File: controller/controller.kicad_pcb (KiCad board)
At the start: 2 copper layers, 14 parts, among them SW1 SW_Push, SW2 SW_Push, SW3 SW_Push, SW4 SW_Push, U1 COM-09032, U2 COM-09032, U3 NRF24L01_Breakout

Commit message: [pcb] controller layout
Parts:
- moved SW2 89.8 mm to (141.4, 79.7)
- moved SW4 88.3 mm to (141.3, 87.4)
- moved SW1 82.7 mm to (131.7, 79.6)
- moved SW3 80.1 mm to (131.6, 87.5)
- moved R3 30.2 mm to (61.7, 69.7)
- moved R2 29.1 mm to (61.9, 63.1)
- moved U1 25.7 mm to (100.1, 94.0)
- moved R1 18.9 mm to (71.8, 57.8)
- moved D1 17.5 mm to (64.4, 56.7)
- moved U2 9.78 mm to (162.6, 105.5)
- moved D2 0.98 mm to (64.4, 63.1)
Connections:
- A1 pad 12: JOY1_V -> NRF_CE
- A1 pad 14: JOY1_H -> unconnected-(A1-GPIO10-Pad14)
- A1 pad 15: JOY2_V -> unconnected-(A1-GPIO11-Pad15)
- A1 pad 16: JOY2_H -> unconnected-(A1-GPIO12-Pad16)
- A1 pad 17: NRF_CE -> unconnected-(A1-GPIO13-Pad17)
- A1 pad 31: unconnected-(A1-GPIO26_ADC0-Pad31) -> JOY1_V
- A1 pad 32: unconnected-(A1-GPIO27_ADC1-Pad32) -> JOY1_H
- A1 pad 34: unconnected-(A1-GPIO28_ADC2-Pad34) -> JOY2_H
- U2 pad V1: +3.3V -> unconnected-(U2-V+-PadV1)
- U2 pad V2: JOY2_V -> unconnected-(U2-V-PadV2)
- U2 pad V3: GND -> unconnected-(U2-V--PadV3)
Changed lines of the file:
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@@
 	(net 19 "BTN1")
 	(net 20 "BTN2")
-	(net 21 "unconnected-(A1-GPIO26_ADC0-Pad31)")
-	(net 22 "unconnected-(A1-GPIO27_ADC1-Pad32)")
+	(net 21 "unconnected-(A1-GPIO12-Pad16)")
+	(net 22 "unconnected-(A1-GPIO13-Pad17)")
 	(net 23 "unconnected-(A1-VSYS-Pad39)")
 	(net 24 "unconnected-(A1-GPIO22-Pad29)")
@@
 	(net 26 "SCK")
 	(net 27 "unconnected-(A1-ADC_VREF-Pad35)")
-	(net 28 "unconnected-(A1-GPIO28_ADC2-Pad34)")
+	(net 28 "unconnected-(A1-GPIO10-Pad14)")
 	(net 29 "unconnected-(A1-VSYS-Pad39)_1")
-	(net 30 "JOY2_V")
+	(net 30 "unconnected-(A1-GPIO11-Pad15)")
 	(net 31 "MOSI")
 	(net 32 "JOY2_BTN")
@@
 	(net 50 "unconnected-(U2-SHIELD__1-PadS2)")
 	(net 51 "unconnected-(U3-IRQ-Pad8)")
+	(net 52 "unconnected-(U2-V+-PadV1)")
+	(net 53 "unconnected-(U2-V-PadV2)")
+	(net 54 "unconnected-(U2-V--PadV3)")
 	(footprint "Button_Switch_THT:SW_PUSH_6mm"
 		(layer "F.Cu")
-		(at 53.4 52.97)
+		(at 131.74 79.61)
 		(descr "Generic 6mm SW tactile push button")
 		(tags "tact sw push 6mm")
@@
 	(footprint "Button_Switch_THT:SW_PUSH_6mm"
 		(layer "F.Cu")
-		(at 53.4 78.62)
+		(at 141.29 87.41)
 		(descr "Generic 6mm SW tactile push button")
 		(tags "tact sw push 6mm")
@@
 	(footprint "Resistor_THT:R_Axial_DIN0204_L3.6mm_D1.6mm_P7.62mm_Horizontal"
 		(layer "F.Cu")
-		(at 89.93 55.67)
+		(at 61.85 63.13)
 		(descr "Resistor, Axial_DIN0204 series, Axial, Horizontal, pin pitch=7.62mm, 0.167W, length*diameter=3.6*1.6mm^2, http://cdn-reichelt.de/documents/datenblatt/B400/1_4W%23YAG.pdf")
 		(tags "Resistor Axial_DIN0204 series Axial Horizontal pin pitch 7.62mm 0.167W length 3.6mm diameter 1.6mm")
@@
 	(footprint "LED_THT:LED_D5.0mm"
 		(layer "F.Cu")
-		(at 64.39 62.15)
+		(at 64.385 63.13)
 		(descr "LED, diameter 5.0mm, 2 pins, http://cdn-reichelt.de/documents/datenblatt/A500/LL-504BC2E-009.pdf, generated by kicad-footprint-generator")
 		(tags "LED")
 		(property "Reference" "D2"
-			(at 1.27 -3.96 0)
+			(at 1.205 -2.64 0)
 			(layer "F.SilkS")
 			(effects
@@
 		(tags "LED")
 		(property "Reference" "D3"
-			(at 1.27 -3.96 0)
+			(at 1.265 -2.98 0)
 			(layer "F.SilkS")
 			(effects
@@
 	(footprint "Resistor_THT:R_Axial_DIN0204_L3.6mm_D1.6mm_P7.62mm_Horizontal"
 		(layer "F.Cu")
-		(at 89.93 58.82)
+		(at 61.74 69.67)
 		(descr "Resistor, Axial_DIN0204 series, Axial, Horizontal, pin pitch=7.62mm, 0.167W, length*diameter=3.6*1.6mm^2, http://cdn-reichelt.de/documents/datenblatt/B400/1_4W%23YAG.pdf")
 		(tags "Resistor Axial_DIN0204 series Axial Horizontal pin pitch 7.62mm 0.167W length 3.6mm diameter 1.6mm")
@@
 	(footprint "Button_Switch_THT:SW_PUSH_6mm"
 		(layer "F.Cu")
-		(at 53.4 61.52)
+		(at 141.36 79.65)
 		(descr "Generic 6mm SW tactile push button")
 		(tags "tact sw push 6mm")
@@
 	(footprint "stuff:XDCR_COM-09032"
 		(layer "F.Cu")
-		(at 124.91 100.55)
+		(at 100.065 93.99)
 		(property "Reference" "U1"
 			(at -2.625 -15.235 0)
@@
 		)
 		(embedded_fonts no)
-		(model "${KIPRJMOD}/libraries/digikey/COM-09032.step"
+		(model "${KIPRJMOD}/libraries/stuff.3dshapes/COM-09032.step"
 			(offset
-				(xyz 0 0 0)
+				(xyz 0 0.5 0)
 			)
 			(scale
@@
 			)
 			(rotate
-				(xyz -90 0 0)
+				(xyz -90 -0 -0)
 			)
 		)
@@
 	(footprint "stuff:XDCR_COM-09032"
 		(layer "F.Cu")
-		(at 172.11 103.06)
+		(at 162.63 105.46)
 		(property "Reference" "U2"
 			(at -2.625 -15.235 0)
@@
 			(layers "*.Cu" "*.Mask")
 			(remove_unused_layers no)
-			(net 25 "+3.3V")
+			(net 52 "unconnected-(U2-V+-PadV1)")
 			(pinfunction "V+")
-			(pintype "passive")
+			(pintype "passive+no_connect")
 			(solder_mask_margin 0.102)
 		)
@@
 			(layers "*.Cu" "*.Mask")
 			(remove_unused_layers no)
-			(net 30 "JOY2_V")
+			(net 53 "unconnected-(U2-V-PadV2)")
 			(pinfunction "V")
-			(pintype "passive")
+			(pintype "passive+no_connect")
 			(solder_mask_margin 0.102)
 		)
@@
 			(layers "*.Cu" "*.Mask")
 			(remove_unused_layers no)
-			(net 6 "GND")
+			(net 54 "unconnected-(U2-V--PadV3)")
 			(pinfunction "V-")
-			(pintype "passive")
+			(pintype "passive+no_connect")
 			(solder_mask_margin 0.102)
 		)
 		(embedded_fonts no)
-		(model "${KIPRJMOD}/libraries/digikey/COM-09032.step"
+		(model "${KIPRJMOD}/libraries/stuff.3dshapes/COM-09032.step"
 			(offset
-				(xyz 0 0 0)
+				(xyz 0 0.5 0)
 			)
 			(scale
@@
 			)
 			(rotate
-				(xyz -90 0 0)
+				(xyz -90 -0 -0)
 			)
 		)
@@
 	(footprint "LED_THT:LED_D5.0mm"
 		(layer "F.Cu")
-		(at 81.48 52.74)
+		(at 64.39 56.71)
 		(descr "LED, diameter 5.0mm, 2 pins, http://cdn-reichelt.de/documents/datenblatt/A500/LL-504BC2E-009.pdf, generated by kicad-footprint-generator")
 		(tags "LED")
@@
 		)
 		(property "Value" "LED"
-			(at 1.27 3.96 0)
+			(at 1.265 4.94 0)
 			(layer "F.Fab")
 			(effects
@@
 	(footprint "Resistor_THT:R_Axial_DIN0204_L3.6mm_D1.6mm_P7.62mm_Horizontal"
 		(layer "F.Cu")
-		(at 89.93 52.52)
+		(at 71.77 57.81)
 		(descr "Resistor, Axial_DIN0204 series, Axial, Horizontal, pin pitch=7.62mm, 0.167W, length*diameter=3.6*1.6mm^2, http://cdn-reichelt.de/documents/datenblatt/B400/1_4W%23YAG.pdf")
 		(tags "Resistor Axial_DIN0204 series Axial Horizontal pin pitch 7.62mm 0.167W length 3.6mm diameter 1.6mm")
@@
 	(footprint "Button_Switch_THT:SW_PUSH_6mm"
 		(layer "F.Cu")
-		(at 53.4 70.07)
+		(at 131.6 87.45)
 		(descr "Generic 6mm SW tactile push button")
 		(tags "tact sw push 6mm")
@@
 			(layers "B.Cu" "B.Mask")
 			(roundrect_rratio 0.5)
-			(net 3 "JOY1_V")
+			(net 9 "NRF_CE")
 			(pinfunction "GPIO9")
 			(pintype "bidirectional")
@@
 			(layers "*.Cu" "*.Mask")
 			(remove_unused_layers no)
-			(net 3 "JOY1_V")
+			(net 9 "NRF_CE")
 			(pinfunction "GPIO9")
 			(pintype "bidirectional")
@@
 			(layers "B.Cu" "B.Mask")
 			(roundrect_rratio 0.5)
-			(net 17 "JOY1_H")
+			(net 28 "unconnected-(A1-GPIO10-Pad14)")
 			(pinfunction "GPIO10")
 			(pintype "bidirectional")
@@
 			(layers "*.Cu" "*.Mask")
 			(remove_unused_layers no)
-			(net 17 "JOY1_H")
+			(net 28 "unconnected-(A1-GPIO10-Pad14)")
 			(pinfunction "GPIO10")
 			(pintype "bidirectional")
@@
 			(layers "B.Cu" "B.Mask")
 			(roundrect_rratio 0.5)
-			(net 30 "JOY2_V")
+			(net 30 "unconnected-(A1-GPIO11-Pad15)")
 			(pinfunction "GPIO11")
 			(pintype "bidirectional")
@@
 			(layers "*.Cu" "*.Mask")
 			(remove_unused_layers no)
-			(net 30 "JOY2_V")
+			(net 30 "unconnected-(A1-GPIO11-Pad15)")
 			(pinfunction "GPIO11")
 			(pintype "bidirectional")
@@
 			(layers "B.Cu" "B.Mask")
 			(roundrect_rratio 0.5)
-			(net 8 "JOY2_H")
+			(net 21 "unconnected-(A1-GPIO12-Pad16)")
 			(pinfunction "GPIO12")
 			(pintype "bidirectional")
@@
 			(layers "*.Cu" "*.Mask")
 			(remove_unused_layers no)
-			(net 8 "JOY2_H")
+			(net 21 "unconnected-(A1-GPIO12-Pad16)")
 			(pinfunction "GPIO12")
 			(pintype "bidirectional")
@@
 			(layers "B.Cu" "B.Mask")
 			(roundrect_rratio 0.5)
-			(net 9 "NRF_CE")
+			(net 22 "unconnected-(A1-GPIO13-Pad17)")
 			(pinfunction "GPIO13")
 			(pintype "bidirectional")
@@
 			(layers "*.Cu" "*.Mask")
 			(remove_unused_layers no)
-			(net 9 "NRF_CE")
+			(net 22 "unconnected-(A1-GPIO13-Pad17)")
 			(pinfunction "GPIO13")
 			(pintype "bidirectional")
@@
 			(layers "*.Cu" "*.Mask")
 			(remove_unused_layers no)
-			(net 21 "unconnected-(A1-GPIO26_ADC0-Pad31)")
+			(net 3 "JOY1_V")
 			(pinfunction "GPIO26_ADC0")
 			(pintype "bidirectional")
@@
 			(layers "B.Cu" "B.Mask")
 			(roundrect_rratio 0.5)
-			(net 21 "unconnected-(A1-GPIO26_ADC0-Pad31)")
+			(net 3 "JOY1_V")
 			(pinfunction "GPIO26_ADC0")
 			(pintype "bidirectional")
@@
 			(layers "*.Cu" "*.Mask")
 			(remove_unused_layers no)
-			(net 22 "unconnected-(A1-GPIO27_ADC1-Pad32)")
+			(net 17 "JOY1_H")
 			(pinfunction "GPIO27_ADC1")
 			(pintype "bidirectional")
@@
 			(layers "B.Cu" "B.Mask")
 			(roundrect_rratio 0.5)
-			(net 22 "unconnected-(A1-GPIO27_ADC1-Pad32)")
+			(net 17 "JOY1_H")
 			(pinfunction "GPIO27_ADC1")
 			(pintype "bidirectional")
@@
 			(layers "*.Cu" "*.Mask")
 			(remove_unused_layers no)
-			(net 28 "unconnected-(A1-GPIO28_ADC2-Pad34)")
+			(net 8 "JOY2_H")
 			(pinfunction "GPIO28_ADC2")
 			(pintype "bidirectional")
@@
 			(layers "B.Cu" "B.Mask")
 			(roundrect_rratio 0.5)
-			(net 28 "unconnected-(A1-GPIO28_ADC2-Pad34)")
+			(net 8 "JOY2_H")
 			(pinfunction "GPIO28_ADC2")
 			(pintype "bidirectional")

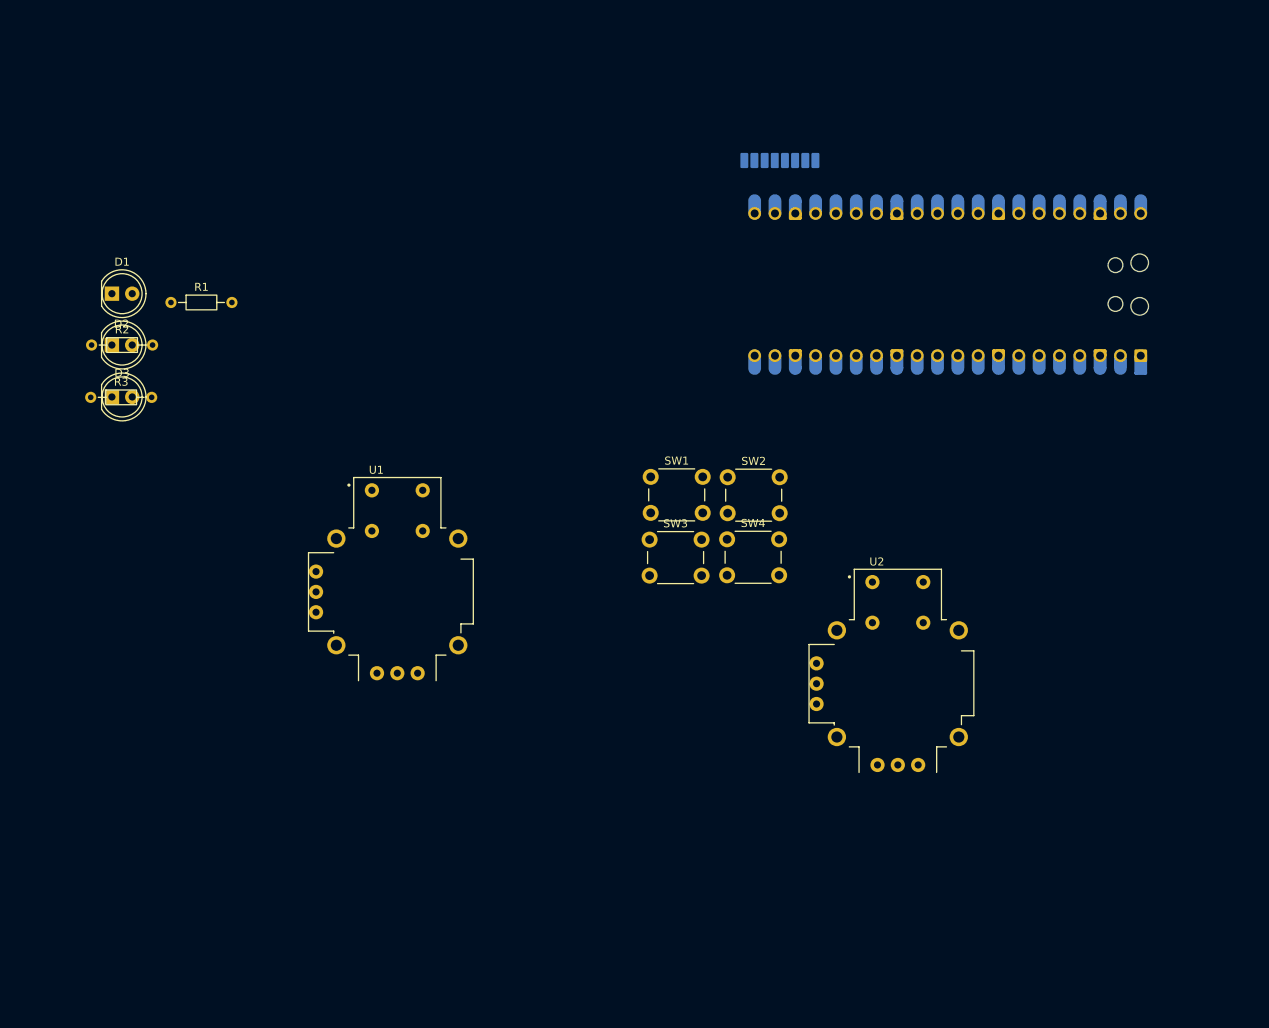
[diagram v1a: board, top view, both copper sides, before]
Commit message: [pcb] change pico for c3 supermini and use priority encoder for more inputs
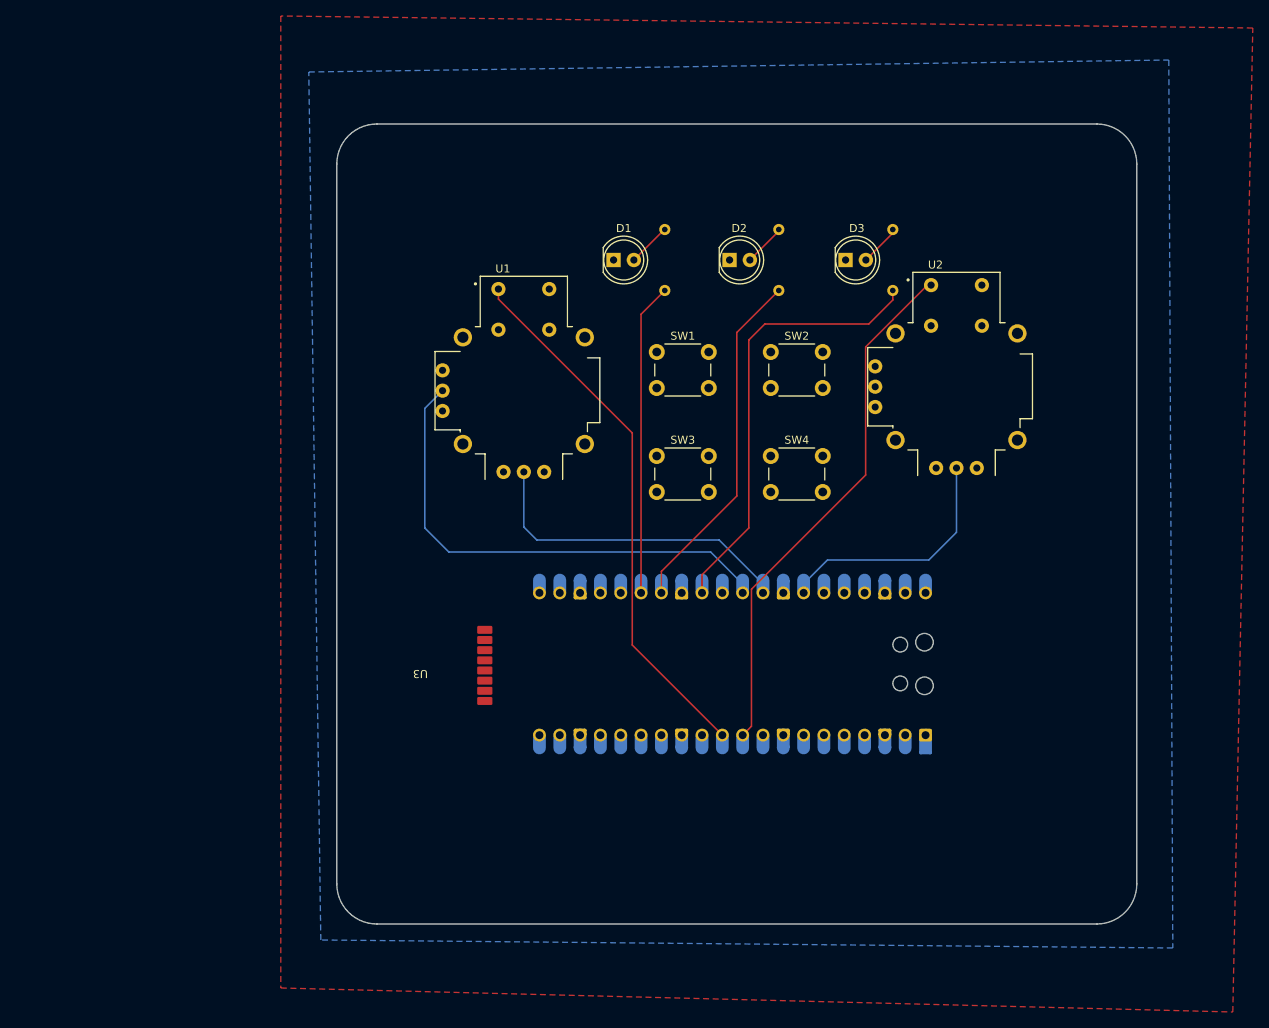
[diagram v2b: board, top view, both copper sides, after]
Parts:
- R1, R2, R3: moved to B.Cu
- U3: moved to F.Cu
- moved R3 102.4 mm to (162.0, 48.7), turned to -90 degrees
- moved D3 93.3 mm to (156.1, 52.5)
- moved R2 87.1 mm to (147.8, 48.7), turned to -90 degrees
- moved U3 84.9 mm to (103.0, 103.7), turned to 180 degrees
- moved D2 77.9 mm to (141.6, 52.5)
- moved D1 62.8 mm to (127.1, 52.5)
- moved R1 62.4 mm to (133.5, 48.7), turned to -90 degrees
- moved A1 54.5 mm to (142.0, 103.0)
- moved U2 37.8 mm to (170.0, 68.3)
- moved U1 29.7 mm to (115.9, 68.8)
- moved SW2 16.6 mm to (146.7, 64.0)
- moved SW1 15.6 mm to (132.5, 64.0)
- moved SW4 11.8 mm to (146.7, 77.0)
- moved SW3 10.5 mm to (132.5, 77.0)
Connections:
- A1 pad 1: LED1 -> unconnected-(A1-GPIO0-Pad1)
- A1 pad 10: JOY1_BTN -> JOY2_BTN
- A1 pad 11: JOY2_BTN -> JOY1_BTN
- A1 pad 12: NRF_CE -> unconnected-(A1-GPIO9-Pad12)
- A1 pad 16: unconnected-(A1-GPIO12-Pad16) -> NRF_CS
- A1 pad 17: unconnected-(A1-GPIO13-Pad17) -> NRF_CE
- A1 pad 2: LED2 -> unconnected-(A1-GPIO1-Pad2)
- A1 pad 22: NRF_CS -> unconnected-(A1-GPIO17-Pad22)
- A1 pad 26: unconnected-(A1-GPIO20-Pad26) -> LED1
- A1 pad 27: unconnected-(A1-GPIO21-Pad27) -> LED2
- A1 pad 29: unconnected-(A1-GPIO22-Pad29) -> LED3
- A1 pad 4: LED3 -> unconnected-(A1-GPIO2-Pad4)
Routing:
- net JOY1_BTN: track 0.00 -> 67.4 mm
- net JOY2_BTN: track 0.00 -> 66.3 mm
- net JOY1_V: track 0.00 -> 61.8 mm
- net LED3: track 0.00 -> 55.3 mm
- net LED2: track 0.00 -> 43.9 mm
- net JOY1_H: track 0.00 -> 40.9 mm
- net LED1: track 0.00 -> 39.0 mm
- net JOY2_H: track 0.00 -> 30.9 mm
- net Net-(D1-A): track 0.00 -> 5.50 mm
- net Net-(D2-A): track 0.00 -> 5.31 mm
- net Net-(D3-A): track 0.00 -> 5.20 mm
- added copper zone on F.Cu, net +3.3V
- added copper zone on B.Cu, net GND
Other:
- board outline added: 100 x 100 mm

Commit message: [pcb] finish controller schematic, route controller pcb
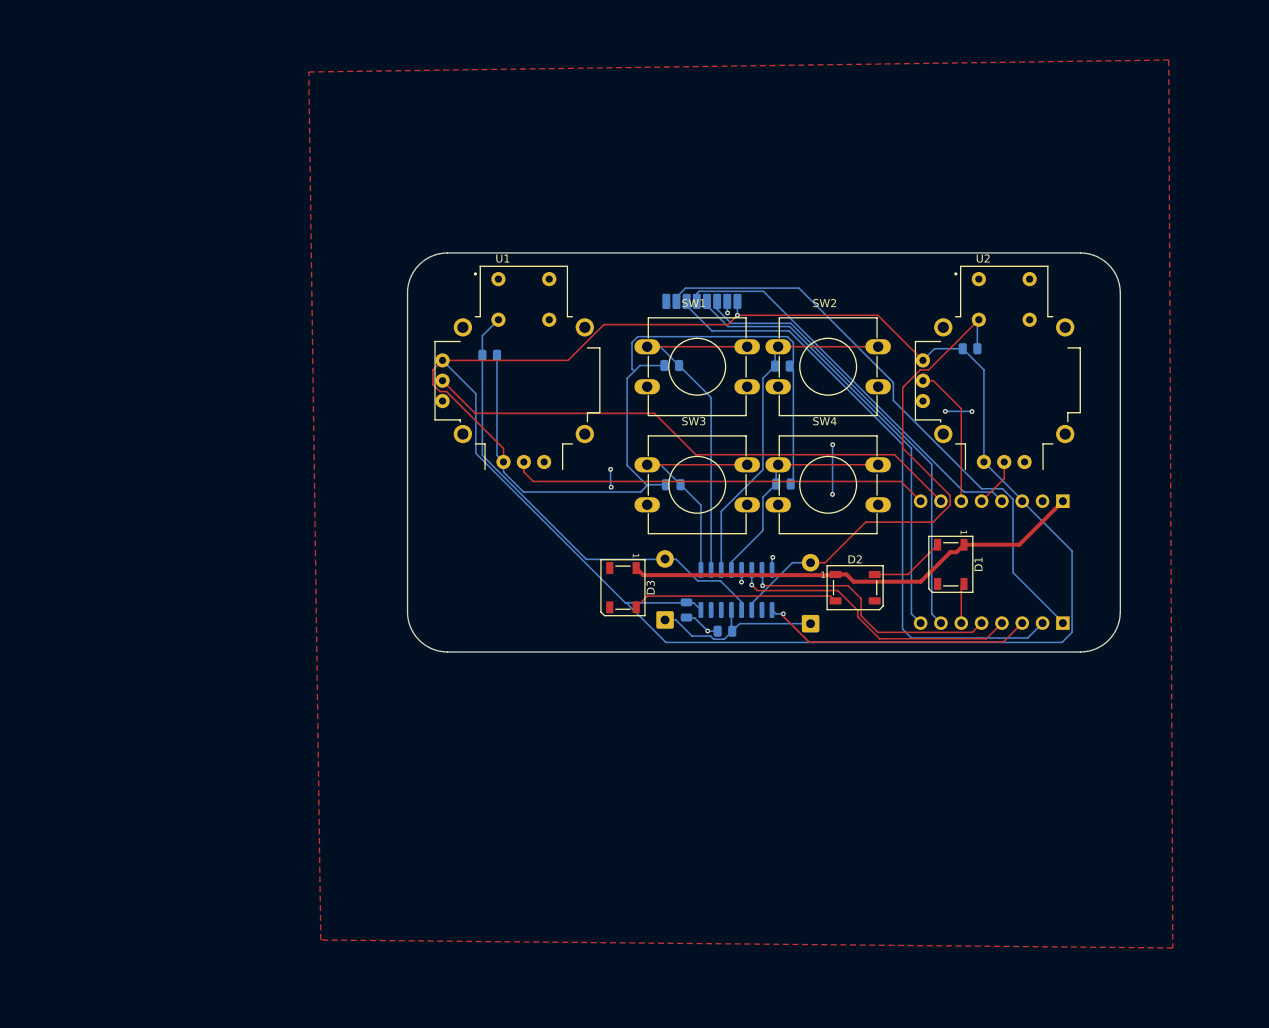
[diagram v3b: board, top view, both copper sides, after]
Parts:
- removed A1: RaspberryPi_Pico, Module:RaspberryPi_Pico_Common_Unspecified
- added C1: 10uF, Capacitor_SMD:C_0805_2012Metric, B.Cu at (136.2, 96.2)
- added D4: 1N5819WS, Diode_THT:D_DO-41_SOD81_P7.62mm_Horizontal, B.Cu at (133.5, 97.5)
- added D5: 1N5819WS, Diode_THT:D_DO-41_SOD81_P7.62mm_Horizontal, B.Cu at (151.7, 98.0)
- added R4: 10K, Resistor_SMD:R_0805_2012Metric, B.Cu at (148.3, 80.5)
- added R5: 10K, Resistor_SMD:R_0805_2012Metric, B.Cu at (111.6, 64.4)
- added R6: 10K, Resistor_SMD:R_0805_2012Metric, B.Cu at (171.7, 63.6)
- added R8: 10K, Resistor_SMD:R_0805_2012Metric, B.Cu at (141.0, 98.9)
- added U4: ESP32C3-SUPERMINI, stuff:ESP32-C3-SuperMini, B.Cu at (174.1, 90.3)
- added U5: 74HC148, Package_SO:SOP-16_3.9x9.9mm_P1.27mm, B.Cu at (142.5, 93.8)
- D1, D2, D3: value LED -> WS2812B; footprint LED_THT:LED_D5.0mm -> LED_SMD:LED_WS2812B_PLCC4_5.0x5.0mm_P3.2mm
- R1, R2, R3: value 1k -> 10K; footprint Resistor_THT:R_Axial_DIN0204_L3.6mm_D1.6mm_P7.62mm_Horizontal -> Resistor_SMD:R_0805_2012Metric
- SW1, SW2, SW3, SW4: footprint Button_Switch_THT:SW_PUSH_6mm -> Button_Switch_THT:SW_PUSH-12mm
- U3: moved to B.Cu
- moved U3 64.8 mm to (138.7, 49.6), turned to 90 degrees
- moved D1 56.8 mm to (169.2, 90.5), turned to -90 degrees
- moved D3 49.5 mm to (128.3, 93.5), turned to -90 degrees
- moved D2 43.9 mm to (157.3, 93.5)
- moved R3 42.1 mm to (134.6, 80.6), turned to 180 degrees
- moved R2 17.1 mm to (148.2, 65.8), turned to 0 degrees
- moved R1 17.0 mm to (134.4, 65.7), turned to 180 degrees
- moved U2 6.02 mm to (175.9, 67.6)
- moved SW3 1.62 mm to (131.3, 78.1)
- moved SW4 1.44 mm to (147.7, 78.1)
- moved SW1 1.37 mm to (131.3, 63.3)
- moved U1 1.24 mm to (115.9, 67.6)
- moved SW2 1.14 mm to (147.7, 63.3)
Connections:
- D1 pad 1: GND -> +5V
- D1 pad 2: Net-(D1-A) -> Net-(D1-DOUT)
- D2 pad 1: GND -> +5V
- D2 pad 2: Net-(D2-A) -> Net-(D2-DOUT)
- D3 pad 1: GND -> +5V
- D3 pad 2: Net-(D3-A) -> unconnected-(D3-DOUT-Pad2)
- R1 pad 1: Net-(D1-A) -> BTN_1
- R1 pad 2: LED1 -> +3.3V
- R2 pad 1: Net-(D2-A) -> BTN_2
- R2 pad 2: LED2 -> +3.3V
- R3 pad 1: Net-(D3-A) -> BTN_3
- R3 pad 2: LED3 -> +3.3V
- SW1 pad 1: GND -> BTN_1
- SW1 pad 2: BTN1 -> GND
- SW2 pad 1: GND -> BTN_2
- SW2 pad 2: BTN2 -> GND
- SW3 pad 1: GND -> BTN_3
- SW3 pad 2: BTN3 -> GND
- SW4 pad 1: GND -> BTN_4
- SW4 pad 2: BTN4 -> GND
- U1 pad B1A: JOY1_BTN -> GND
- U1 pad B2A: GND -> BTN_JOY_L
- U2 pad B1A: JOY2_BTN -> GND
- U2 pad B2A: GND -> BTN_JOY_R
- U2 pad V1: unconnected-(U2-V+-PadV1) -> +3.3V
- U2 pad V2: unconnected-(U2-V-PadV2) -> JOY2_V
- U2 pad V3: unconnected-(U2-V--PadV3) -> GND
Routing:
- net +3.3V: track 0.00 -> 338.1 mm, vias 0 -> 1
- net MOSI: track 0.00 -> 76.5 mm
- net MISO: track 0.00 -> 73.4 mm
- net JOY1_BTN: track 67.4 -> 0.00 mm
- net JOY2_BTN: track 66.3 -> 0.00 mm
- net BTN_JOY_R: track 0.00 -> 64.6 mm
- net BTN_JOY_L: track 0.00 -> 58.8 mm
- net +5V: track 0.00 -> 58.3 mm
- net NRF_CE: track 0.00 -> 56.2 mm
- net NRF_CS: track 0.00 -> 55.8 mm
- net LED3: track 55.3 -> 0.00 mm
- net SCK: track 0.00 -> 50.1 mm
- net BTN_1: track 0.00 -> 44.7 mm
- net LED2: track 43.9 -> 0.00 mm
- net BTN_2: track 0.00 -> 43.4 mm
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- added copper zone on F.Cu, net GND
- removed copper zone on F.Cu, net +3.3V
- removed copper zone on B.Cu, net GND
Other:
- board size 100 x 100 mm -> 89.1 x 49.9 mm
